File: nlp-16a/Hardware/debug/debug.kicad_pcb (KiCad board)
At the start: 2 copper layers, 69.8 x 61.6 mm, 16 parts, among them J1 Conn_01x06_Male, J2 Conn_01x06_Female, J3 Conn_01x06_Female, J4 Conn_02x20_Odd_Even, J5 Conn_02x10_Odd_Even, J6 Conn_02x10_Odd_Even, J7 Conn_02x10_Odd_Even, J8 Conn_02x10_Odd_Even, U1 CH32V003F4P6

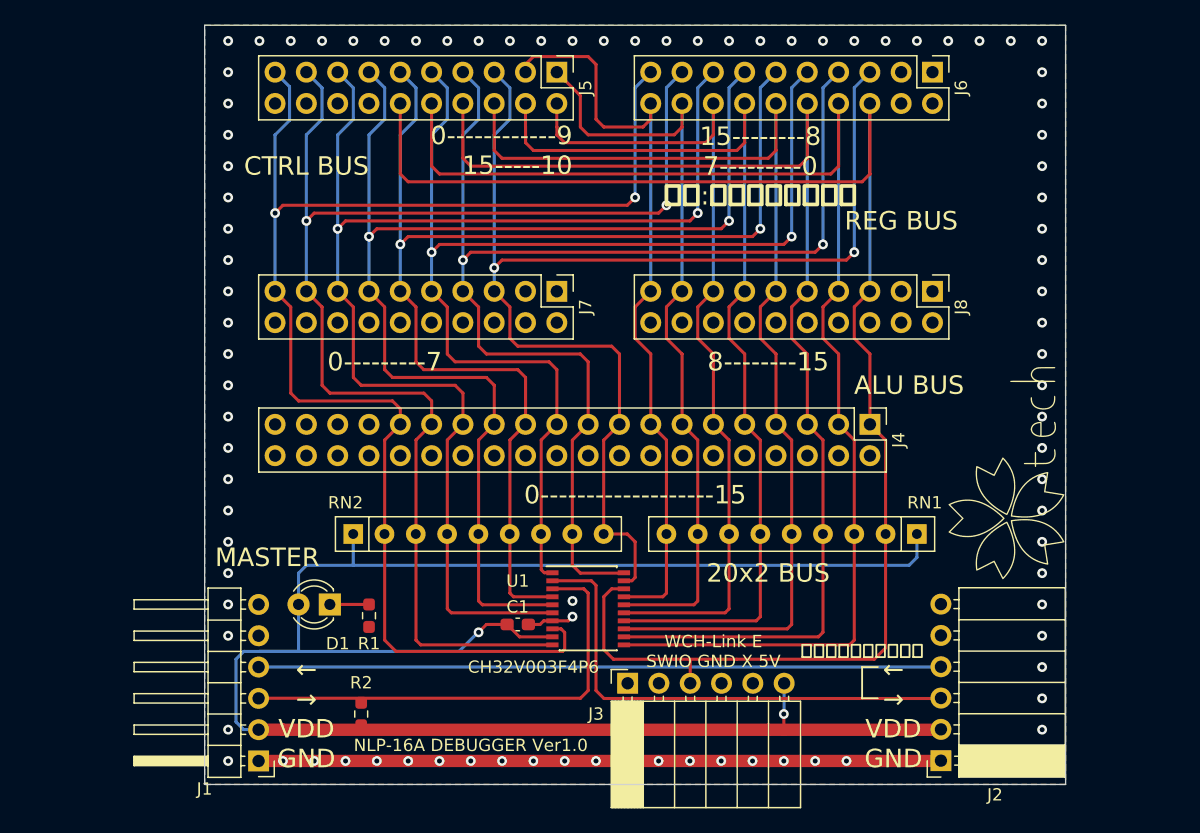
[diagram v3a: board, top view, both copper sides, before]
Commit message: v1.1全ガーバーを更新
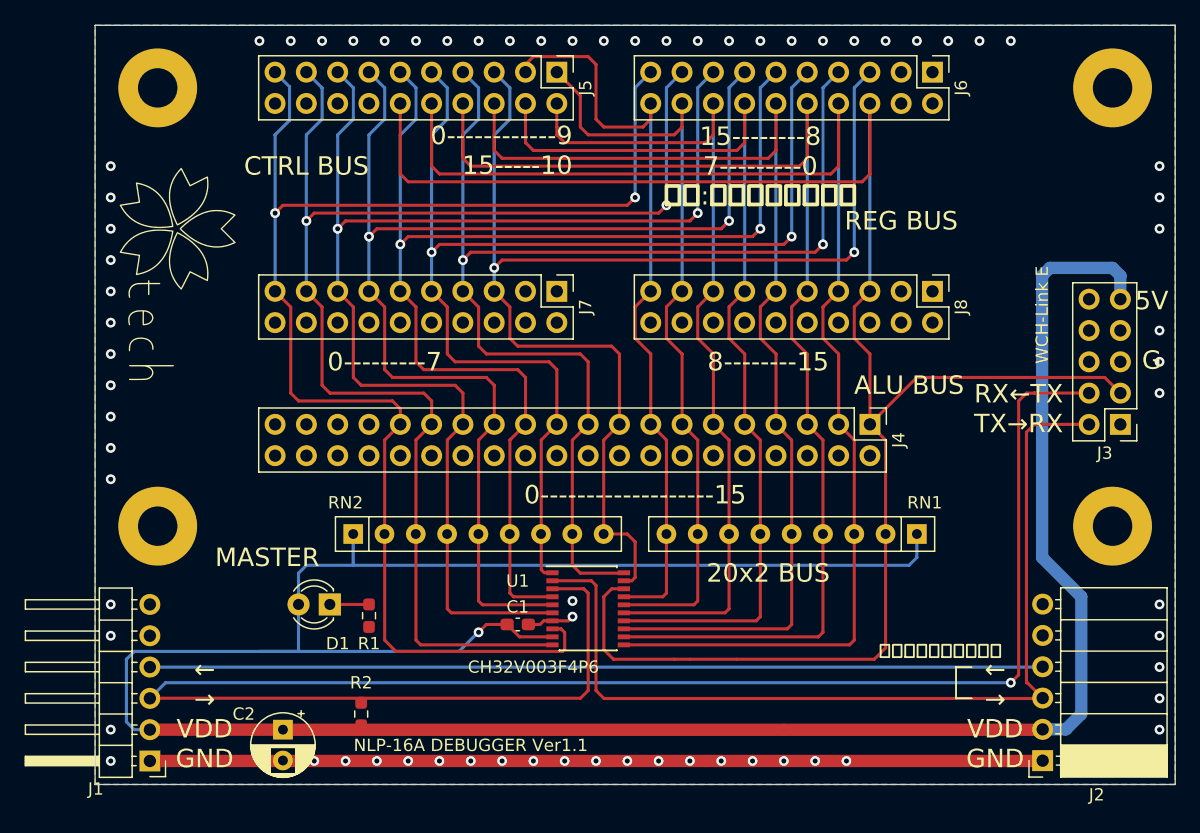
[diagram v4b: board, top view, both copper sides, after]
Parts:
- added C2: C_Polarized, Capacitor_THT:CP_Radial_D5.0mm_P2.50mm, F.Cu at (125.1, 125.7)
- added H1: MountingHole_Pad, MountingHole:MountingHole_3.2mm_M3_Pad, F.Cu at (114.9, 109.2)
- added H2: MountingHole_Pad, MountingHole:MountingHole_3.2mm_M3_Pad, F.Cu at (114.9, 73.7)
- added H3: MountingHole_Pad, MountingHole:MountingHole_3.2mm_M3_Pad, F.Cu at (192.4, 109.2)
- added H4: MountingHole_Pad, MountingHole:MountingHole_3.2mm_M3_Pad, F.Cu at (192.4, 73.7)
- J3: value Conn_01x06_Female -> Conn_02x05_Odd_Even; footprint Connector_PinSocket_2.54mm:PinSocket_1x06_P2.54mm_Horizontal -> Connector_PinHeader_2.54mm:PinHeader_2x05_P2.54mm_Vertical
- moved G*** 69.5 mm to (116.2, 89.5), turned to -90 degrees
- moved J3 45.2 mm to (193.0, 101.0), turned to 180 degrees
- moved J1 8.82 mm to (114.3, 128.3)
- moved J2 8.26 mm to (186.7, 128.2)
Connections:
- net DATA15 renamed SWDIO
- J1 pad 3: Net-(J1-Pad3) -> RX
- J2 pad 3: Net-(J2-Pad3) -> TX
- J3 pad 2: unconnected-(J3-Pad2) -> TX
- J3 pad 4: GND -> RX
- J3 pad 5: unconnected-(J3-Pad5) -> GND
- J3 pad 6: VDD -> unconnected-(J3-Pad6)
- R2 pad 1: Net-(J1-Pad3) -> RX
- U1 pad 2: Net-(J2-Pad3) -> TX
- U1 pad 3: Net-(J1-Pad3) -> RX
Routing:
- net RX: track 0.00 -> 146.3 mm, vias 0 -> 1
- net TX: track 0.00 -> 76.2 mm
- net VDD: track 158.2 -> 229.8 mm, vias 2 -> 1
- net Net-(J2-Pad3): track 40.4 -> 0.00 mm
- net Net-(J1-Pad3): track 37.9 -> 0.00 mm
- net SWDIO: track 127.5 -> 148.0 mm
- net GND: track 59.2 -> 76.3 mm, vias 92 -> 72
- net Net-(J1-Pad4): track 55.3 -> 72.4 mm
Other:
- board size 69.8 x 61.6 mm -> 87.6 x 61.6 mm
- board text added: "5V G"
- board text added: "NLP-16A DEBUGGER Ver1.1"
- board text added: "RX←TX TX→RX"
- board text added: "WCH-Link E"
- board text removed: "NLP-16A DEBUGGER Ver1.0"
- board text removed: "WCH-Link E SWIO GND X 5V"

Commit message: デバッガ改良
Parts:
- added J9: Conn_01x02_Male, Connector_PinHeader_2.54mm:PinHeader_1x02_P2.54mm_Vertical, F.Cu at (179.1, 118.1)
- moved G*** 61.8 mm to (167.6, 123.8), turned to 0 degrees
- moved R2 2.57 mm to (131.1, 121.9), turned to 0 degrees
- moved C2 2.48 mm to (125.1, 123.3)
- moved C1 1.27 mm to (142.9, 117.2)
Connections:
- J1 pad 2: VDD -> unconnected-(J1-Pad2)
- J1 pad 3: RX -> VDD
- J1 pad 4: Net-(J1-Pad4) -> RX
- J1 pad 5: unconnected-(J1-Pad5) -> Net-(J1-Pad5)
- J2 pad 2: VDD -> unconnected-(J2-Pad2)
- J2 pad 3: TX -> VDD
- J2 pad 4: Net-(J1-Pad4) -> TX
- J2 pad 5: unconnected-(J2-Pad5) -> Net-(J1-Pad5)
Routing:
- net Net-(J1-Pad5): track 0.00 -> 74.5 mm
- net Net-(J1-Pad4): track 72.4 -> 0.00 mm
- net TX: track 76.2 -> 71.1 mm
- net RX: track 146.3 -> 143.5 mm
- net GND: track 76.3 -> 77.6 mm, vias 72 -> 71
- net VDD: track 229.8 -> 230.8 mm
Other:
- board text added: "0---------7 LSB"
- board text added: "15--------8 7---------0"
- board text added: "2x10 BUS"
- board text added: "2x20 BUS"
- board text added: "8--------15 MSB"
- board text added: "X ← → VDD X GND"
- board text added: "末端ではジャンパする"
- board text added: "注意:逆順モードを使用"
- board text removed: "0---------7"
- board text removed: "15--------8 7---------0 注意:逆順モードを使用"
- board text removed: "20x2 BUS"
- board text removed: "8--------15"
- board text removed: "REG BUS"
- board text removed: "← → VDD GND"
- board text removed: "末端ではショートする"
